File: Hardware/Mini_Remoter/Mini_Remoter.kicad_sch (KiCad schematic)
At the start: 27 parts

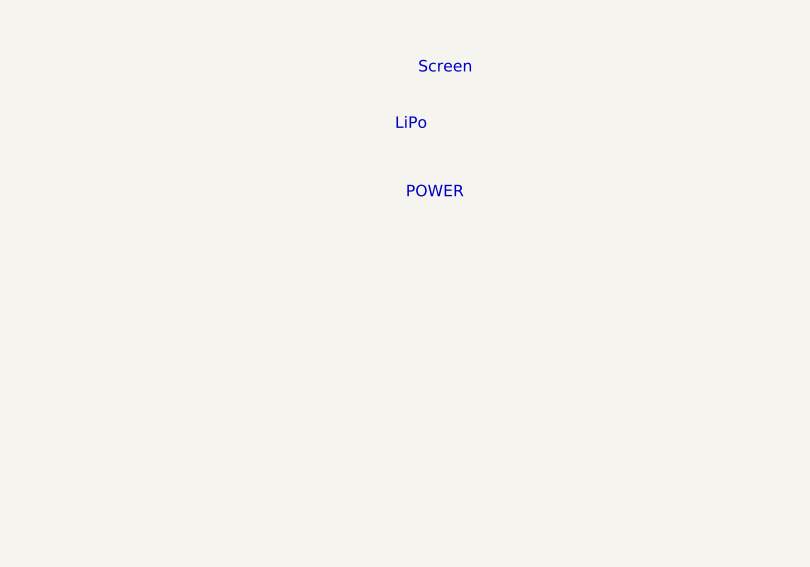
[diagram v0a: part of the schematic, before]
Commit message: 遥控器硬件文档添加IMU说明
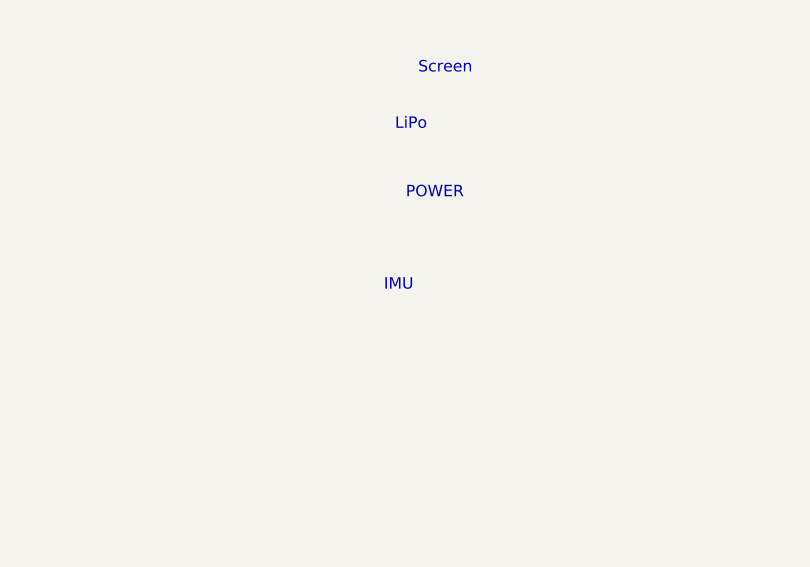
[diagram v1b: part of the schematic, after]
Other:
- note added: "IMU"
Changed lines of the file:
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@@
+    (effects (font (size 1.27 1.27)) (justify left bottom))
+  )
+  (text "IMU" (at 80.01 147.32 0)
     (effects (font (size 1.27 1.27)) (justify left bottom))
   )

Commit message: 开始拟制迷你遥控器设计方案，原理图待完善
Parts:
- removed J? (x5): Conn_01x01_Female, Del:Conn_2.54_01x01_STAMP, symbol Connector:Conn_01x01_Female
- added C? (x9): 100nF, symbol Device:C
- added C? (x2): 9pF, symbol Device:C
- added C?: 10uF, symbol Device:C
- added D? (x2): LED, symbol Device:LED
- added J?: Conn_01x02_Male, symbol Connector:Conn_01x02_Male
- added J?: Conn_01x06_Female, symbol Connector:Conn_01x06_Female
- added R? (x2): 2.2K, symbol Device:R
- added R?: 10K, symbol Device:R
- added R?: 1M, symbol Device:R
- added SW? (x3): KEY, symbol Del_Schlib:KEY
- added SW? (x2): KEY, Del:SW_2x4x3.5_SIDE, symbol Del_Schlib:KEY
- added U?: ATmega328P-A, Package_QFP:TQFP-32_7x7mm_P0.8mm, symbol MCU_Microchip_ATmega:ATmega328P-A
- added U?: CH340K, Del:ESSOP-10_P1.0_3.9, symbol Del_Schlib:CH340K
- added U?: XC6206PxxxMR, Package_TO_SOT_SMD:SOT-23, symbol Regulator_Linear:XC6206PxxxMR
- added Y?: 16MHz, Crystal:Crystal_SMD_3225-4Pin_3.2x2.5mm, symbol Device:Crystal_GND24
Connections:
- net +5V: now also J?.1, J?.1, J?.6, J?.6, C?.1, C?.1, C?.1, C?.1, J?.1 (Pin_1), R?.1, R?.1, R?.2, U?.18 (AVCC), U?.3 (VI), U?.4 (VCC), U?.6 (VCC)
- net +BATT: now also J?.1 (Pin_1)
- net GND: now also J?.3, J?.3, J?.4, J?.4, U?.8 (GND), C?.1, C?.1, C?.1, C?.2, C?.2, C?.2, C?.2, C?.2, C?.2, C?.2, C?.2, D?.1 (K), J?.6 (Pin_6), SW?.2 (B), SW?.2 (B), SW?.2 (B), SW?.2 (B), SW?.2 (B), U?.1 (GND), U?.11 (EP), U?.21 (GND), U?.3 (GND), U?.3 (GND), U?.5 (GND), Y?.2, Y?.4
- net VBUS: now also C?.2, U?.7 (VCC)
- net A0: now reaches J?.2
- net A0: now also U?.23 (PC0)
- net A1: now reaches J?.5
- net A1: now also U?.24 (PC1)
- net D_P: now reaches USB?.A6 (DP1)
- net D_P: now also USB?.B6 (DP2), U?.1 (UD+)
- net D_N: now reaches USB?.A7 (DN1)
- net D_N: now also USB?.B7 (DN2), U?.2 (UD-)
- net A2: now reaches J?.2
- net A2: now also U?.25 (PC2)
- net A3: now reaches J?.5
- net A3: now also U?.26 (PC3)
- net +3V3: now reaches U?.1 (VCC)
- net +3V3: now also C?.1, C?.1, U?.2 (VO)
- net RF24_CE: now reaches U?.2 (CE)
- net RF24_CSN: now reaches U?.3 (CSN)
- net RF24_SCK: now reaches U?.4 (SCK)
- net RF24_MOSI: now reaches U?.5 (MOSI)
- net RF24_MISO: now reaches U?.6 (MISO)
- net RF24_IRQ: now reaches U?.7 (IRQ)
- new net: J?.2 (Pin_2), SW?.1 (A)
- new net: C?.2, U?.20 (AREF)
- new net: C?.1, R?.1, U?.7 (XTAL1/PB6), Y?.3
- new net: C?.1, R?.2, U?.8 (XTAL2/PB7), Y?.1
- new net: D?.2 (A), R?.2 (x2)
- new net: C?.2, U?.10 (V3)
- new net A4: U?.27 (PC4)
- new net A5: U?.28 (PC5)
- new net DTR: C?.1, U?.4 (DTR#)
- new net KEY_A: SW?.1 (A)
- new net KEY_B: SW?.1 (A)
- new net LED: D?.1 (K)
- new net LEFT_CH: SW?.1 (A)
- new net MISO: J?.3 (Pin_3), U?.16 (PB4)
- new net MOSI: J?.4 (Pin_4), U?.15 (PB3)
- new net PB0: U?.12 (PB0)
- new net PB1: U?.13 (PB1)
- new net PB2: U?.14 (PB2)
- new net PD2: U?.32 (PD2)
- new net PD3: U?.1 (PD3)
- new net PD4: U?.2 (PD4)
- new net PD5: U?.9 (PD5)
- new net PD6: U?.10 (PD6)
- new net PD7: U?.11 (PD7)
- new net RESET: C?.2, J?.5 (Pin_5), R?.1, U?.29 (~{RESET}/PC6)
- new net RIGHT_CH: SW?.1 (A)
- new net RXD: U?.30 (PD0), U?.8 (TXD)
- new net SCK: J?.2 (Pin_2), U?.17 (PB5)
- new net TXD: U?.31 (PD1), U?.9 (RXD)
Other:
- note added: "Li-Charge"
- note added: "MCU-ATMEGA328P"
- note added: "USB-TTL"
- note removed: "IMU"
- note removed: "LiPo"
- note removed: "MCU"
- note removed: "POWER"
- note removed: "USB"
- moved on the sheet: C?, D?, J?, L?, R?, U?, USB?

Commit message: 添加mini遥控器原理图屏幕和蜂鸣器部分
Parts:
- added BZ1: Buzzer, ADel:DET402, symbol Device:Buzzer
- added C11, C4, C6: 1uF, Capacitor_SMD:C_0603_1608Metric_Pad1.08x0.95mm_HandSolder, symbol Device:C
- added C8: 4.7uF, Capacitor_SMD:C_0603_1608Metric_Pad1.08x0.95mm_HandSolder, symbol Device:C
- added C9: 2.2uF, Capacitor_SMD:C_0603_1608Metric_Pad1.08x0.95mm_HandSolder, symbol Device:C
- added D7: D, Diode_SMD:D_SOD-123, symbol Device:D
- added Q1: S8050, Package_TO_SOT_SMD:SOT-23, symbol Device:Q_NPN_BEC
- added R2: 910K, Resistor_SMD:R_0603_1608Metric_Pad0.98x0.95mm_HandSolder, symbol Device:R
- added R6: 100R, Resistor_SMD:R_0603_1608Metric_Pad0.98x0.95mm_HandSolder, symbol Device:R
- added R7: 10K, Resistor_SMD:R_0603_1608Metric_Pad0.98x0.95mm_HandSolder, symbol Device:R
- added U2: OLED_SSD1306_30P_096, ADel:OLED_12864_30P_P0.7_HOLE, symbol ADel:OLED_SSD1306_30P_096
- C1, C17, C18, C19, C20, C21, C22, C23, C24, C25, C5, C7: renamed from C?; footprint (none) -> Capacitor_SMD:C_0603_1608Metric_Pad1.08x0.95mm_HandSolder
- D5, D6: renamed from D?; footprint (none) -> LED_SMD:LED_0603_1608Metric_Pad1.05x0.95mm_HandSolder
- J1: renamed from J?; footprint (none) -> ADel:PH2.0mm-2P-WT
- J4: renamed from J?; footprint (none) -> Connector_JST:JST_SHL_SM06B-SHLS-TF_1x06-1MP_P1.00mm_Horizontal
- R10, R11, R4, R5: renamed from R?; footprint (none) -> Resistor_SMD:R_0603_1608Metric_Pad0.98x0.95mm_HandSolder
- SW3, SW4: renamed from SW?; footprint (none) -> ADel:BUTTON_SWITCH_4x4
- SW5: renamed from SW?; footprint (none) -> ADel:SELFLOCK_SWITCH
- gave numbers to parts that had none: 28
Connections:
- net +3V3: now also C11.2, U2.6 (VBAT), U2.9 (VDD)
- net +5V: now also BZ1.1 (-), D7.1 (K)
- net GND: now also C11.1, C8.1, C9.1, Q1.2 (E), R2.1, R7.1, U2.1 (NC), U2.10 (BS0), U2.11 (BS1), U2.12 (BS2), U2.16 (R/W#), U2.17 (E/RD#), U2.21 (D3), U2.22 (D4), U2.23 (D5), U2.24 (D6), U2.25 (D7), U2.29 (VLSS), U2.30 (NC), U2.8 (VSS)
- new net: BZ1.2 (+), D7.2 (A), Q1.3 (C)
- new net: Q1.1 (B), R6.2, R7.2
- new net: C9.2, U2.28 (VCC)
- new net: C8.2, U2.27 (VCOMH)
- new net: C6.1, U2.5 (C1N)
- new net: C6.2, U2.4 (C1P)
- new net: C4.2, U2.2 (C2P)
- new net: R2.2, U2.26 (IREF)
- new net: C4.1, U2.3 (C2N)
- new net BUZZ: R6.1
- new net OLED_CS: U2.13 (CS#)
- new net OLED_DC: U2.15 (DC)
- new net OLED_MOSI: U2.19 (D1)
- new net OLED_RES: U2.14 (RES#)
- new net OLED_SCK: U2.18 (D0)
- no-connect marks 6 -> 9
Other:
- note added: "BUZZ"
- note added: "SCREEN"
- note removed: "Screen"
- moved on the sheet: C1, C10, C12, C13, C14, C15, C16, C17, C18, C19, C2, C20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

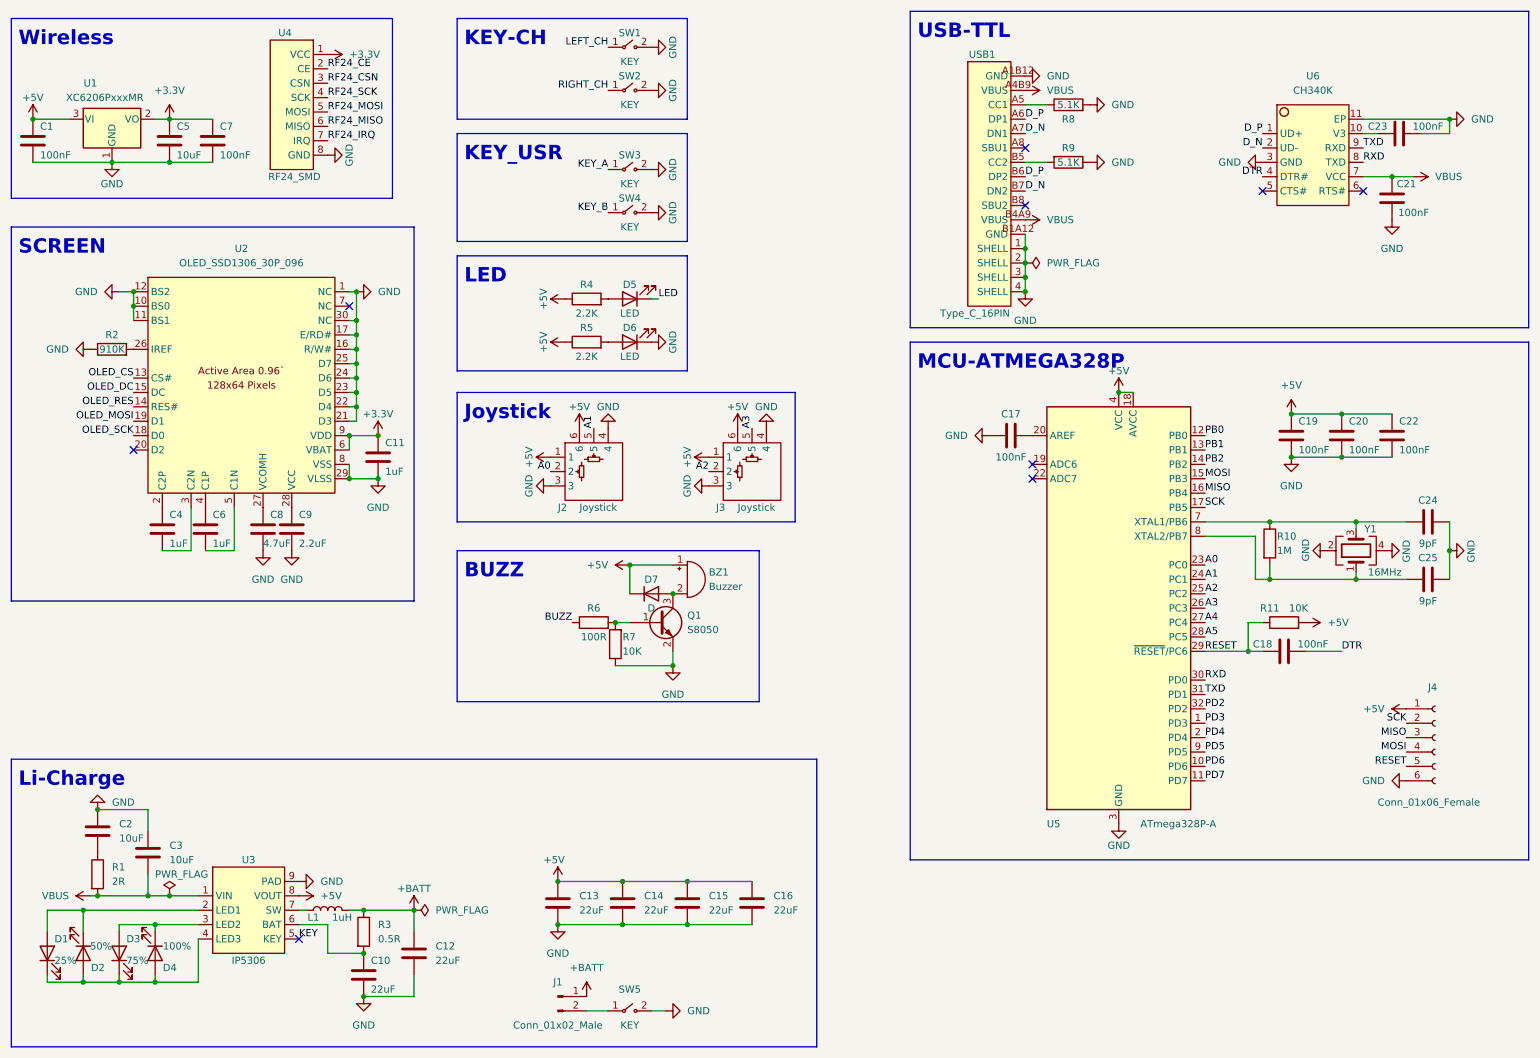
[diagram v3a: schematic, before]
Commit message: 完成Mini遥控器PCB初版设计，等待打板验证，开始设计外壳
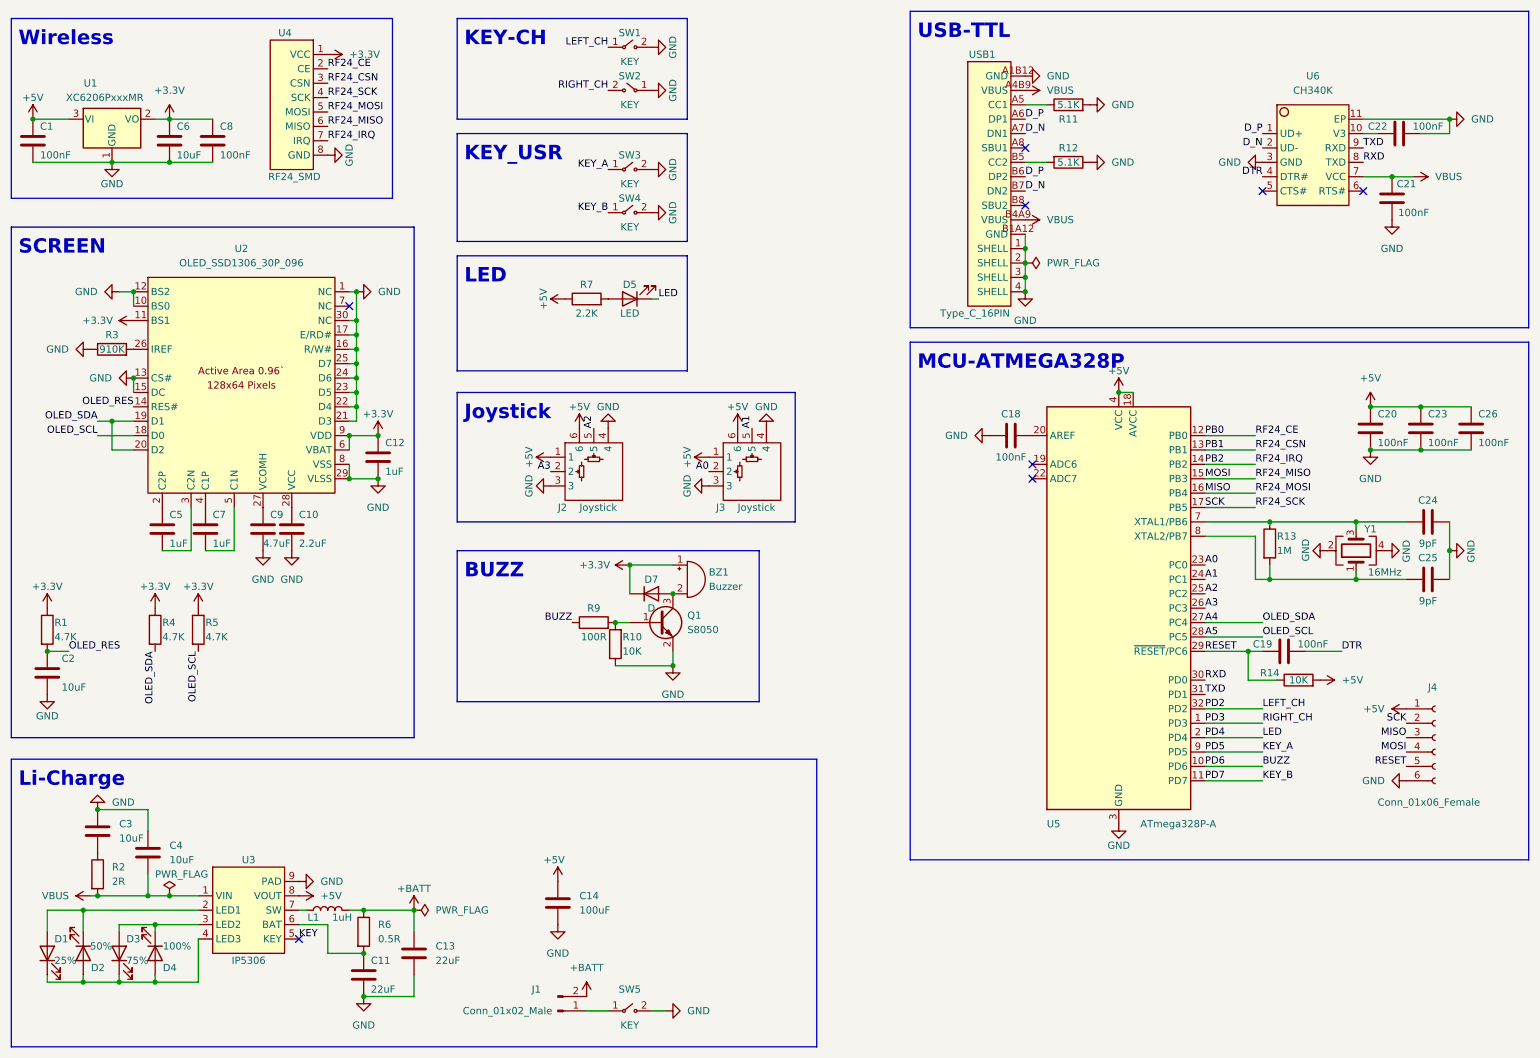
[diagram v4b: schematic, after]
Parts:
- removed C14, C15, C16: 22uF, Capacitor_SMD:C_1206_3216Metric, symbol Device:C
- removed D6: LED, LED_SMD:LED_0603_1608Metric_Pad1.05x0.95mm_HandSolder, symbol Device:LED
- added C2: 10uF, Capacitor_SMD:C_0603_1608Metric_Pad1.08x0.95mm_HandSolder, symbol Device:C
- added R1, R4: 4.7K, Resistor_SMD:R_0603_1608Metric_Pad0.98x0.95mm_HandSolder, symbol Device:R
- C14: renamed from C13; value 22uF -> 100uF; footprint Capacitor_SMD:C_1206_3216Metric -> Capacitor_SMD:C_1210_3225Metric
- J2, J3: footprint Del:PSP_JOYSTICK -> ADel:PSP_JOYSTICK
- L1: footprint Del:IND0420 -> ADel:IND0420
- R5: value 2.2K -> 4.7K
- SW1, SW2: footprint Del:SW_2x4x3.5_SIDE -> ADel:SW_2x4x3.5_SIDE
- U4: footprint Del:RF24_SMD -> ADel:RF24_SMD
- U6: footprint Del:ESSOP-10_P1.0_3.9 -> ADel:ESSOP-10_P1.0_3.9
- USB1: footprint Del:TYPE-C-16PIN_SMD -> ADel:TYPE-C-16PIN_SMD
- renumbered C9 to C10, C10 to C11, C11 to C12, C12 to C13, C17 to C18, C18 to C19, C19 to C20, C23 to C22, C20 to C23, C22 to C26, C2 to C3, C3 to C4, C4 to C5, C5 to C6, C6 to C7, C7 to C8, C8 to C9, R7 to R10, R8 to R11, R9 to R12, R10 to R13, R11 to R14, R1 to R2, R2 to R3, R3 to R6, R4 to R7, R6 to R9
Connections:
- net OLED_CS is gone; now on net GND: U2.13 (CS#)
- net OLED_DC is gone; now on net GND: U2.15 (DC)
- net OLED_MOSI is gone; now on net A4: U2.19 (D1)
- net OLED_SCK is gone; now on net A5: U2.18 (D0)
- net PD2 is gone; now on net LEFT_CH: U5.32 (PD2)
- net PD4 is gone; now on net LED: U5.2 (PD4)
- net PD5 is gone; now on net KEY_A: U5.9 (PD5)
- net PD6 is gone; now on net BUZZ: U5.10 (PD6)
- net PD7 is gone; now on net KEY_B: U5.11 (PD7)
- net RF24_CE is gone; now on net PB0: U4.2 (CE)
- net RF24_CSN is gone; now on net PB1: U4.3 (CSN)
- net RF24_IRQ is gone; now on net PB2: U4.7 (IRQ)
- net RF24_MISO is gone; now on net MOSI: U4.6 (MISO)
- net RF24_MOSI is gone; now on net MISO: U4.5 (MOSI)
- net RIGHT_CH is gone; now on net GND: SW2.1 (A)
- net SCK is gone; now on net RF24_SCK: J4.2 (Pin_2), U5.17 (PB5)
- net +3V3: now also BZ1.1 (-), D7.1 (K), R5.1, U2.11 (BS1), R1.1, R4.1
- net +5V: no longer BZ1.1 (-), D7.1 (K), R5.1
- net +BATT: now also J1.2 (Pin_2); no longer J1.1 (Pin_1)
- net A0: now also J3.2; no longer J2.2
- net A1: now also J3.5; no longer J2.5
- net A2: now also J2.5; no longer J3.2
- net A3: now also J2.2; no longer J3.5
- net A4: now also U2.20 (D2), R4.2
- net A5: now also R5.2
- net GND: now also C2.2; no longer SW2.2 (B), U2.11 (BS1)
- net OLED_RES: now also C2.1, R1.2
- net PD3: now also SW2.2 (B)
- net at SW5.1 (A): now also J1.1 (Pin_1); no longer J1.2 (Pin_2)
- no-connect marks 9 -> 8
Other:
- moved on the sheet: C20, C23, C26, R14
